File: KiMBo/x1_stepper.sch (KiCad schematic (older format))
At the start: 23 parts, among them U26 TMC2130

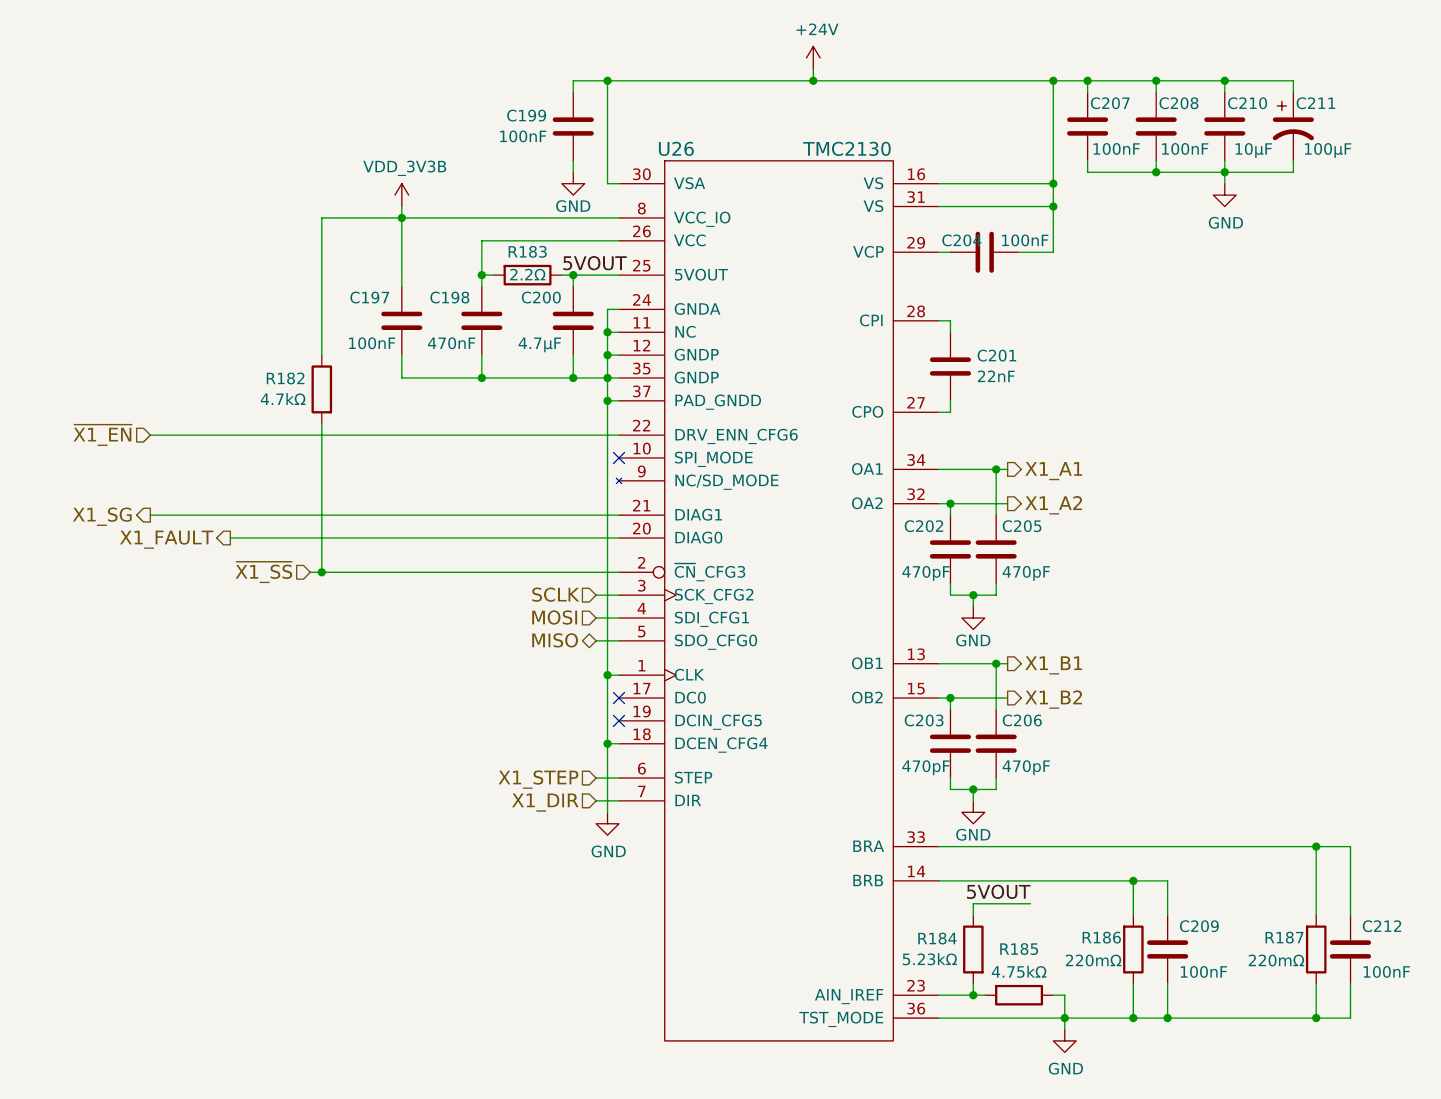
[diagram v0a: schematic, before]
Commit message: Leave SPI0 free for a display, reassign pins so SPI1 is available
Fix some typos/errors
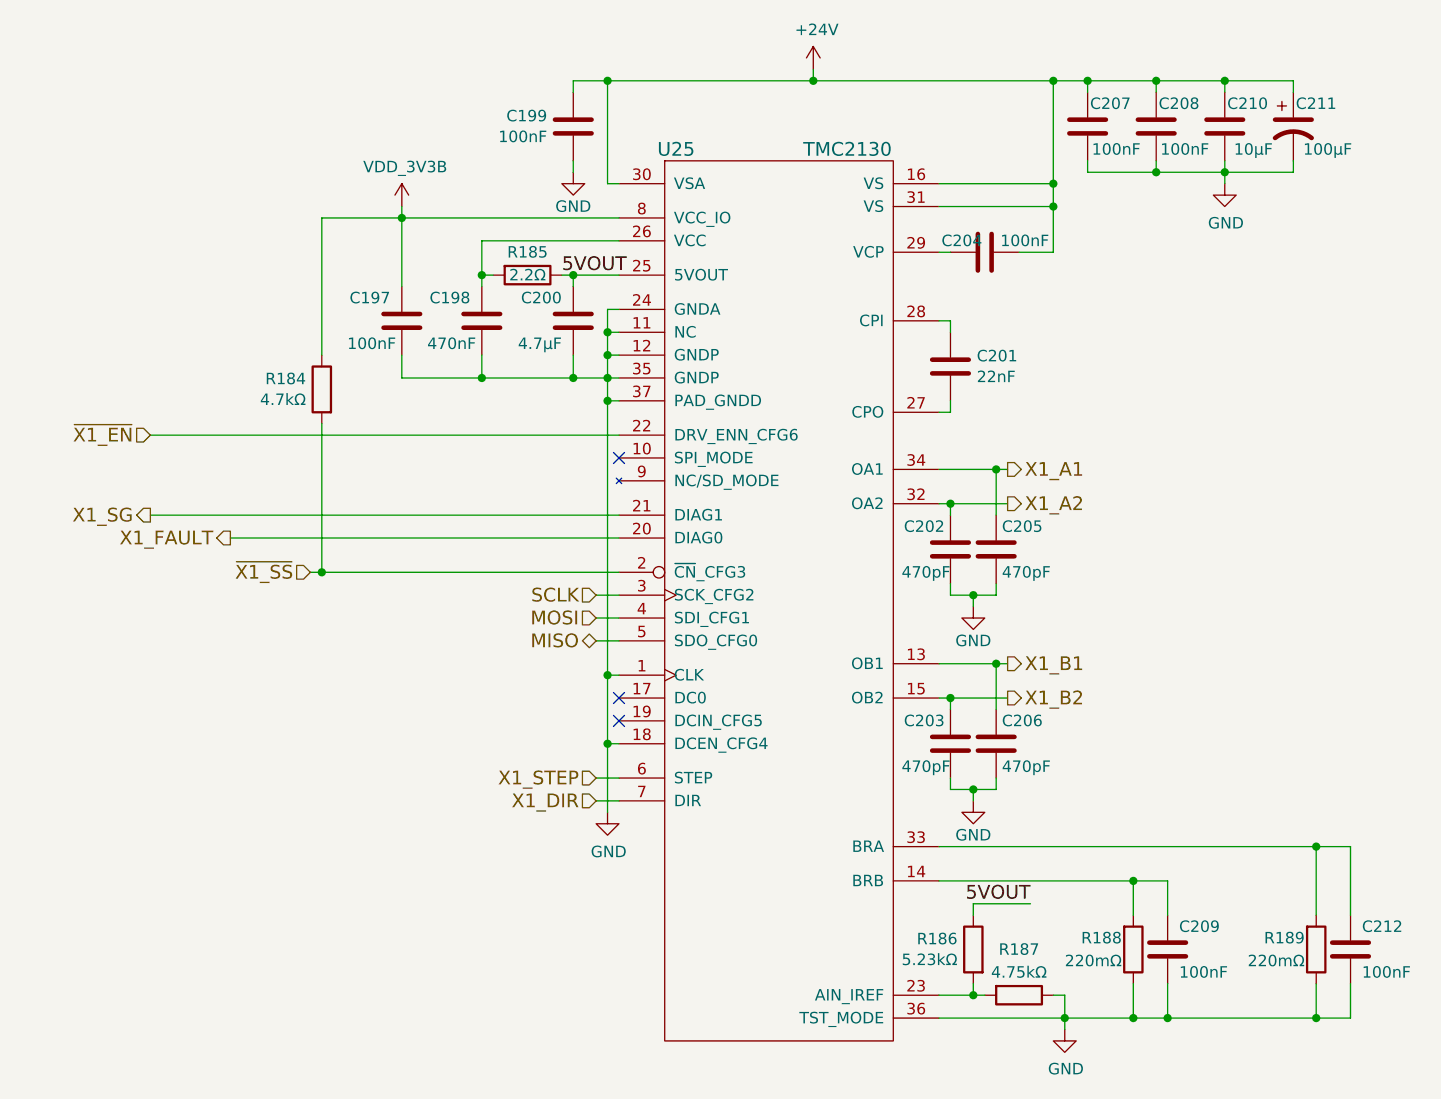
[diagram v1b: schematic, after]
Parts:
- renumbered R182 to R184, R183 to R185, R184 to R186, R185 to R187, R186 to R188, R187 to R189, U26 to U25
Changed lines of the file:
@@
 $EndComp
 $Comp
-L GND #PWR0256
+L GND #PWR0255
 U 1 1 5BA7E13F
 P 7500 3300
-F 0 "#PWR0256" H 7500 3050 50  0001 C CNN
+F 0 "#PWR0255" H 7500 3050 50  0001 C CNN
 F 1 "GND" H 7500 3150 50  0000 C CNN
 F 2 "" H 7500 3300 50  0000 C CNN
@@
 $EndComp
 $Comp
-L GND #PWR0257
+L GND #PWR0256
 U 1 1 58C092DF
 P 10350 3350
-F 0 "#PWR0257" H 10350 3100 50  0001 C CNN
+F 0 "#PWR0256" H 10350 3100 50  0001 C CNN
 F 1 "GND" H 10355 3177 50  0000 C CNN
 F 2 "" H 10350 3350 50  0000 C CNN
@@
 $EndComp
 $Comp
-L +24V #PWR0258
+L +24V #PWR0257
 U 1 1 5BA7E142
 P 8550 2850
-F 0 "#PWR0258" H 8550 2700 50  0001 C CNN
+F 0 "#PWR0257" H 8550 2700 50  0001 C CNN
 F 1 "+24V" H 8565 3023 50  0000 C CNN
 F 2 "" H 8550 2850 50  0000 C CNN
@@
 $EndComp
 $Comp
-L R R187
+L R R189
 U 1 1 5BA7E144
 P 10750 6700
-F 0 "R187" H 10700 6650 50  0000 R CNN
+F 0 "R189" H 10700 6650 50  0000 R CNN
 F 1 "220mΩ" H 10700 6750 50  0000 R CNN
 F 2 "" V 10680 6700 50  0001 C CNN
@@
 $EndComp
 $Comp
-L R R186
+L R R188
 U 1 1 5BA7E145
 P 9950 6700
-F 0 "R186" H 9900 6650 50  0000 R CNN
+F 0 "R188" H 9900 6650 50  0000 R CNN
 F 1 "220mΩ" H 9900 6750 50  0000 R CNN
 F 2 "" V 9880 6700 50  0001 C CNN
@@
 $EndComp
 $Comp
-L GND #PWR0259
+L GND #PWR0258
 U 1 1 58C09300
 P 9650 7050
-F 0 "#PWR0259" H 9650 6800 50  0001 C CNN
+F 0 "#PWR0258" H 9650 6800 50  0001 C CNN
 F 1 "GND" H 9655 6877 50  0000 C CNN
 F 2 "" H 9650 7050 50  0000 C CNN
@@
 NoConn ~ 7700 5600
 $Comp
-L R R183
+L R R185
 U 1 1 58C09307
 P 7300 3750
-F 0 "R183" V 7200 3750 50  0000 C CNN
+F 0 "R185" V 7200 3750 50  0000 C CNN
 F 1 "2.2Ω" V 7300 3750 50  0000 C CNN
 F 2 "" V 7230 3750 50  0001 C CNN
@@
 NoConn ~ 7700 5700
 $Comp
-L GND #PWR0260
+L GND #PWR0259
 U 1 1 58C09323
 P 7650 6100
-F 0 "#PWR0260" H 7650 5850 50  0001 C CNN
+F 0 "#PWR0259" H 7650 5850 50  0001 C CNN
 F 1 "GND" H 7655 5927 50  0000 C CNN
 F 2 "" H 7650 6100 50  0000 C CNN
@@
 5VOUT
 $Comp
-L R R184
+L R R186
 U 1 1 58C09343
 P 9250 6700
-F 0 "R184" H 9319 6746 50  0000 L CNN
+F 0 "R186" H 9319 6746 50  0000 L CNN
 F 1 "5.23kΩ" H 9319 6655 50  0000 L CNN
 F 2 "" V 9180 6700 50  0001 C CNN
@@
 5VOUT
 $Comp
-L R R185
+L R R187
 U 1 1 58C0934B
 P 9450 6900
-F 0 "R185" V 9250 6900 50  0000 C CNN
+F 0 "R187" V 9250 6900 50  0000 C CNN
 F 1 "4.75kΩ" V 9350 6900 50  0000 C CNN
 F 2 "" V 9380 6900 50  0001 C CNN
@@
 $EndComp
 $Comp
-L R R182
+L R R184
 U 1 1 5BA7E14F
 P 6400 4250
-F 0 "R182" H 6469 4296 50  0000 L CNN
+F 0 "R184" H 6469 4296 50  0000 L CNN
 F 1 "4.7kΩ" H 6469 4205 50  0000 L CNN
 F 2 "" V 6330 4250 50  0001 C CNN
@@
 $EndComp
 $Comp
-L GND #PWR0261
+L GND #PWR0260
 U 1 1 5BA7E152
 P 9250 5200
-F 0 "#PWR0261" H 9250 4950 50  0001 C CNN
+F 0 "#PWR0260" H 9250 4950 50  0001 C CNN
 F 1 "GND" H 9250 5050 50  0000 C CNN
 F 2 "" H 9250 5200 50  0000 C CNN
@@
 $EndComp
 $Comp
-L GND #PWR0262
+L GND #PWR0261
 U 1 1 5BA7E155
 P 9250 6050
-F 0 "#PWR0262" H 9250 5800 50  0001 C CNN
+F 0 "#PWR0261" H 9250 5800 50  0001 C CNN
 F 1 "GND" H 9250 5900 50  0000 C CNN
 F 2 "" H 9250 6050 50  0000 C CNN
@@
 $EndComp
 $Comp
-L TMC2130 U26
+L TMC2130 U25
 U 1 1 5BA7E157
 P 8400 4700
-F 0 "U26" H 7950 6200 60  0000 C CNN
+F 0 "U25" H 7950 6200 60  0000 C CNN
 F 1 "TMC2130" H 8700 6200 60  0000 C CNN
 F 2 "" H 8400 5000 60  0001 C CNN
@@
 	6400 3500 7700 3500
 $Comp
-L VDD_3V3B #PWR0263
+L VDD_3V3B #PWR0262
 U 1 1 5BA7E15A
 P 6750 3450
-F 0 "#PWR0263" H 6750 3300 50  0001 C CNN
+F 0 "#PWR0262" H 6750 3300 50  0001 C CNN
 F 1 "VDD_3V3B" H 6765 3623 50  0000 C CNN
 F 2 "" H 6750 3450 50  0000 C CNN

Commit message: Use fixed 5V LM2592HV Buck, include SPI0 header for LCD
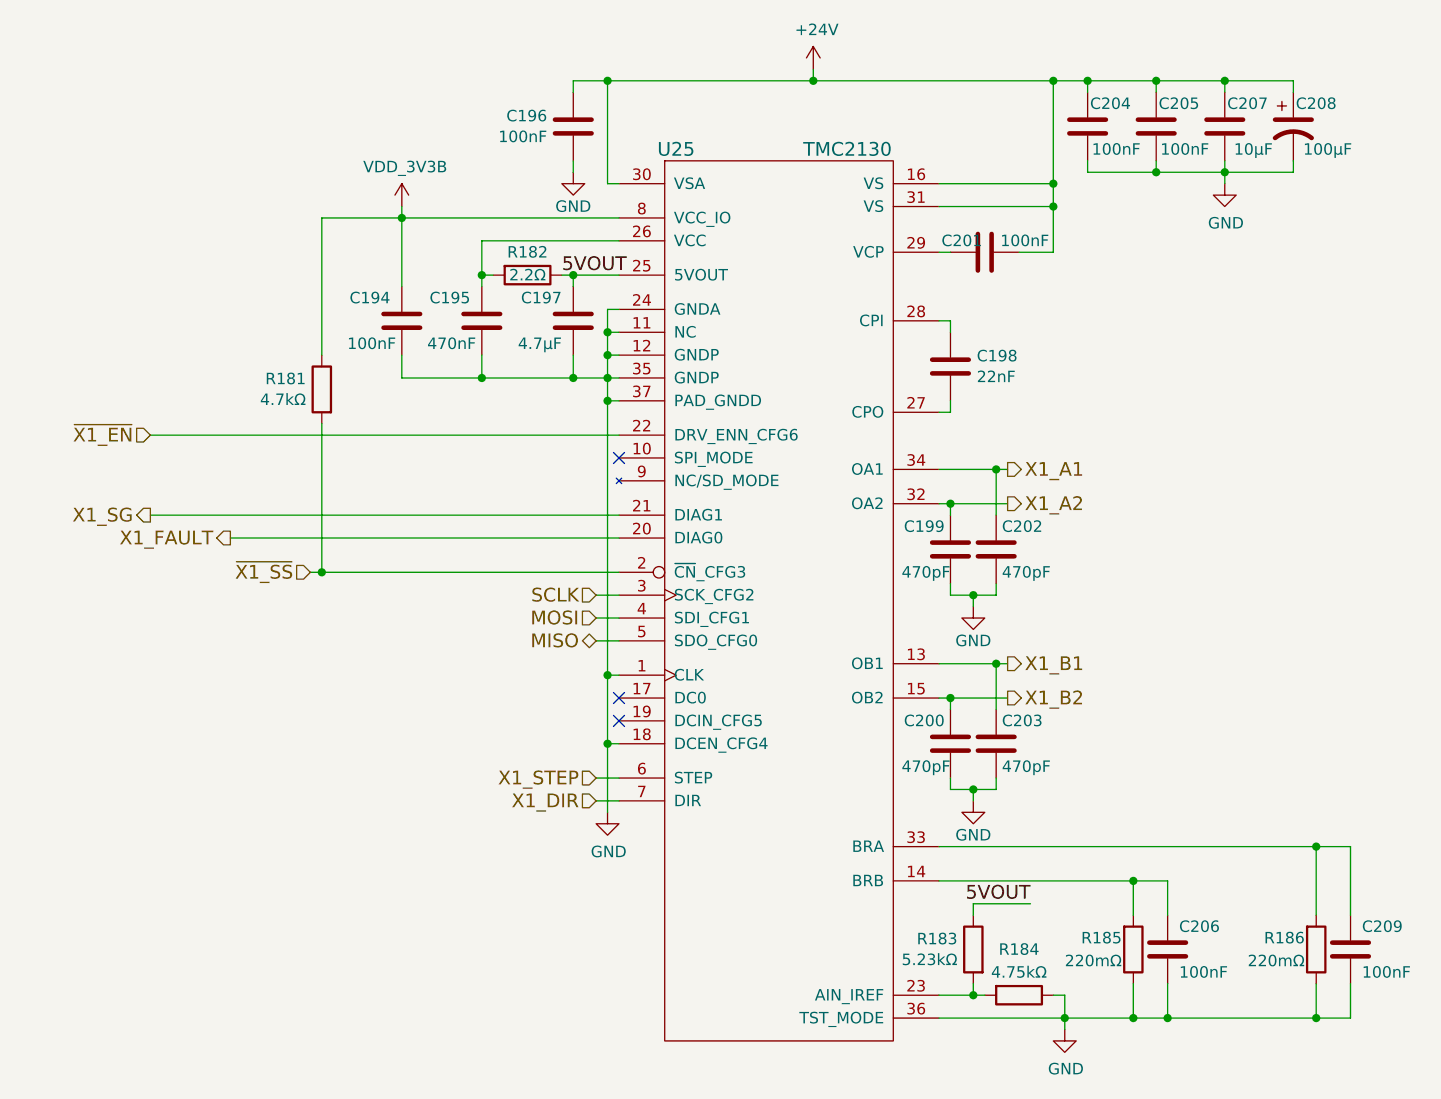
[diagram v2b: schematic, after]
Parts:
- renumbered C197 to C194, C198 to C195, C199 to C196, C200 to C197, C201 to C198, C202 to C199, C203 to C200, C204 to C201, C205 to C202, C206 to C203, C207 to C204, C208 to C205, C209 to C206, C210 to C207, C211 to C208, C212 to C209, R184 to R181, R185 to R182, R186 to R183, R187 to R184, R188 to R185, R189 to R186
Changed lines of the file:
@@
 X1_SG
 $Comp
-L C C199
+L C C196
 U 1 1 58C092B6
 P 7500 3100
-F 0 "C199" H 7386 3054 50  0000 R CNN
+F 0 "C196" H 7386 3054 50  0000 R CNN
 F 1 "100nF" H 7386 3145 50  0000 R CNN
 F 2 "Capacitors_SMD:C_0603" H 7538 2950 50  0001 C CNN
@@
 $EndComp
 $Comp
-L C C204
+L C C201
 U 1 1 58C092BD
 P 9300 3650
-F 0 "C204" V 9250 3550 50  0000 C CNN
+F 0 "C201" V 9250 3550 50  0000 C CNN
 F 1 "100nF" V 9250 3825 50  0000 C CNN
 F 2 "Capacitors_SMD:C_0603" H 9338 3500 50  0001 C CNN
@@
 $EndComp
 $Comp
-L CP1 C211
+L CP1 C208
 U 1 1 5BA7E13D
 P 10650 3100
-F 0 "C211" H 10750 3200 50  0000 C CNN
+F 0 "C208" H 10750 3200 50  0000 C CNN
 F 1 "100μF" H 10800 3000 50  0000 C CNN
 F 2 "Capacitors_SMD:c_elec_8x10" H 10650 3100 50  0001 C CNN
@@
 $EndComp
 $Comp
-L C C207
+L C C204
 U 1 1 5BA7E13E
 P 9750 3100
-F 0 "C207" H 9650 3200 50  0000 C CNN
+F 0 "C204" H 9650 3200 50  0000 C CNN
 F 1 "100nF" H 9625 3000 50  0000 C CNN
 F 2 "Capacitors_SMD:C_0603" H 9788 2950 50  0001 C CNN
@@
 $EndComp
 $Comp
-L GND #PWR0255
+L GND #PWR0250
 U 1 1 5BA7E13F
 P 7500 3300
-F 0 "#PWR0255" H 7500 3050 50  0001 C CNN
+F 0 "#PWR0250" H 7500 3050 50  0001 C CNN
 F 1 "GND" H 7500 3150 50  0000 C CNN
 F 2 "" H 7500 3300 50  0000 C CNN
@@
 $EndComp
 $Comp
-L C C208
+L C C205
 U 1 1 58C092D8
 P 10050 3100
-F 0 "C208" H 9950 3200 50  0000 C CNN
+F 0 "C205" H 9950 3200 50  0000 C CNN
 F 1 "100nF" H 9925 3000 50  0000 C CNN
 F 2 "Capacitors_SMD:C_0603" H 10088 2950 50  0001 C CNN
@@
 $EndComp
 $Comp
-L GND #PWR0256
+L GND #PWR0251
 U 1 1 58C092DF
 P 10350 3350
-F 0 "#PWR0256" H 10350 3100 50  0001 C CNN
+F 0 "#PWR0251" H 10350 3100 50  0001 C CNN
 F 1 "GND" H 10355 3177 50  0000 C CNN
 F 2 "" H 10350 3350 50  0000 C CNN
@@
 $EndComp
 $Comp
-L +24V #PWR0257
+L +24V #PWR0252
 U 1 1 5BA7E142
 P 8550 2850
-F 0 "#PWR0257" H 8550 2700 50  0001 C CNN
+F 0 "#PWR0252" H 8550 2700 50  0001 C CNN
 F 1 "+24V" H 8565 3023 50  0000 C CNN
 F 2 "" H 8550 2850 50  0000 C CNN
@@
 $EndComp
 $Comp
-L C C201
+L C C198
 U 1 1 5BA7E143
 P 9150 4150
-F 0 "C201" H 9265 4196 50  0000 L CNN
+F 0 "C198" H 9265 4196 50  0000 L CNN
 F 1 "22nF" H 9265 4105 50  0000 L CNN
 F 2 "Capacitors_SMD:C_0402" H 9188 4000 50  0001 C CNN
@@
 $EndComp
 $Comp
-L R R189
+L R R186
 U 1 1 5BA7E144
 P 10750 6700
-F 0 "R189" H 10700 6650 50  0000 R CNN
+F 0 "R186" H 10700 6650 50  0000 R CNN
 F 1 "220mΩ" H 10700 6750 50  0000 R CNN
 F 2 "" V 10680 6700 50  0001 C CNN
@@
 $EndComp
 $Comp
-L R R188
+L R R185
 U 1 1 5BA7E145
 P 9950 6700
-F 0 "R188" H 9900 6650 50  0000 R CNN
+F 0 "R185" H 9900 6650 50  0000 R CNN
 F 1 "220mΩ" H 9900 6750 50  0000 R CNN
 F 2 "" V 9880 6700 50  0001 C CNN
@@
 $EndComp
 $Comp
-L GND #PWR0258
+L GND #PWR0253
 U 1 1 58C09300
 P 9650 7050
-F 0 "#PWR0258" H 9650 6800 50  0001 C CNN
+F 0 "#PWR0253" H 9650 6800 50  0001 C CNN
 F 1 "GND" H 9655 6877 50  0000 C CNN
 F 2 "" H 9650 7050 50  0000 C CNN
@@
 NoConn ~ 7700 5600
 $Comp
-L R R185
+L R R182
 U 1 1 58C09307
 P 7300 3750
-F 0 "R185" V 7200 3750 50  0000 C CNN
+F 0 "R182" V 7200 3750 50  0000 C CNN
 F 1 "2.2Ω" V 7300 3750 50  0000 C CNN
 F 2 "" V 7230 3750 50  0001 C CNN
@@
 $EndComp
 $Comp
-L C C198
+L C C195
 U 1 1 58C0930E
 P 7100 3950
-F 0 "C198" H 7150 4050 50  0000 L CNN
+F 0 "C195" H 7150 4050 50  0000 L CNN
 F 1 "470nF" H 7125 3850 50  0000 L CNN
 F 2 "Capacitors_SMD:C_0603" H 7138 3800 50  0001 C CNN
@@
 NoConn ~ 7700 5700
 $Comp
-L GND #PWR0259
+L GND #PWR0254
 U 1 1 58C09323
 P 7650 6100
-F 0 "#PWR0259" H 7650 5850 50  0001 C CNN
+F 0 "#PWR0254" H 7650 5850 50  0001 C CNN
 F 1 "GND" H 7655 5927 50  0000 C CNN
 F 2 "" H 7650 6100 50  0000 C CNN
@@
 $EndComp
 $Comp
-L C C209
+L C C206
 U 1 1 58C09329
 P 10100 6700
-F 0 "C209" H 10150 6800 50  0000 L CNN
+F 0 "C206" H 10150 6800 50  0000 L CNN
 F 1 "100nF" H 10150 6600 50  0000 L CNN
 F 2 "Capacitors_SMD:C_0603" H 10138 6550 50  0001 C CNN
@@
 NoConn ~ 7700 4550
 $Comp
-L C C200
+L C C197
 U 1 1 58C0933B
 P 7500 3950
-F 0 "C200" H 7550 4050 50  0000 L CNN
+F 0 "C197" H 7550 4050 50  0000 L CNN
 F 1 "4.7μF" H 7550 3850 50  0000 L CNN
 F 2 "Capacitors_SMD:C_0402" H 7538 3800 50  0001 C CNN
@@
 5VOUT
 $Comp
-L R R186
+L R R183
 U 1 1 58C09343
 P 9250 6700
-F 0 "R186" H 9319 6746 50  0000 L CNN
+F 0 "R183" H 9319 6746 50  0000 L CNN
 F 1 "5.23kΩ" H 9319 6655 50  0000 L CNN
 F 2 "" V 9180 6700 50  0001 C CNN
@@
 5VOUT
 $Comp
-L R R187
+L R R184
 U 1 1 58C0934B
 P 9450 6900
-F 0 "R187" V 9250 6900 50  0000 C CNN
+F 0 "R184" V 9250 6900 50  0000 C CNN
 F 1 "4.75kΩ" V 9350 6900 50  0000 C CNN
 F 2 "" V 9380 6900 50  0001 C CNN
@@
 $EndComp
 $Comp
-L R R184
+L R R181
 U 1 1 5BA7E14F
 P 6400 4250
-F 0 "R184" H 6469 4296 50  0000 L CNN
+F 0 "R181" H 6469 4296 50  0000 L CNN
 F 1 "4.7kΩ" H 6469 4205 50  0000 L CNN
 F 2 "" V 6330 4250 50  0001 C CNN
@@
 $EndComp
 $Comp
-L C C212
+L C C209
 U 1 1 5BA7E150
 P 10900 6700
-F 0 "C212" H 10950 6800 50  0000 L CNN
+F 0 "C209" H 10950 6800 50  0000 L CNN
 F 1 "100nF" H 10950 6600 50  0000 L CNN
 F 2 "Capacitors_SMD:C_0603" H 10938 6550 50  0001 C CNN
@@
 $EndComp
 $Comp
-L C C202
+L C C199
 U 1 1 5BA7E151
 P 9150 4950
-F 0 "C202" H 9175 5050 50  0000 L CNN
+F 0 "C199" H 9175 5050 50  0000 L CNN
 F 1 "470pF" H 9150 4850 50  0000 L CNN
 F 2 "Capacitors_SMD:C_0603" H 9188 4800 50  0001 C CNN
@@
 $EndComp
 $Comp
-L GND #PWR0260
+L GND #PWR0255
 U 1 1 5BA7E152
 P 9250 5200
-F 0 "#PWR0260" H 9250 4950 50  0001 C CNN
+F 0 "#PWR0255" H 9250 4950 50  0001 C CNN
 F 1 "GND" H 9250 5050 50  0000 C CNN
 F 2 "" H 9250 5200 50  0000 C CNN
@@
 $EndComp
 $Comp
-L C C205
+L C C202
 U 1 1 5BA7E153
 P 9350 4950
-F 0 "C205" H 9375 5050 50  0000 L CNN
+F 0 "C202" H 9375 5050 50  0000 L CNN
 F 1 "470pF" H 9375 4850 50  0000 L CNN
 F 2 "Capacitors_SMD:C_0603" H 9388 4800 50  0001 C CNN
@@
 $EndComp
 $Comp
-L C C203
+L C C200
 U 1 1 58C09377
 P 9150 5800
-F 0 "C203" H 9175 5900 50  0000 L CNN
+F 0 "C200" H 9175 5900 50  0000 L CNN
 F 1 "470pF" H 9150 5700 50  0000 L CNN
 F 2 "Capacitors_SMD:C_0603" H 9188 5650 50  0001 C CNN
@@
 $EndComp
 $Comp
-L GND #PWR0261
+L GND #PWR0256
 U 1 1 5BA7E155
 P 9250 6050
-F 0 "#PWR0261" H 9250 5800 50  0001 C CNN
+F 0 "#PWR0256" H 9250 5800 50  0001 C CNN
 F 1 "GND" H 9250 5900 50  0000 C CNN
 F 2 "" H 9250 6050 50  0000 C CNN
@@
 $EndComp
 $Comp
-L C C206
+L C C203
 U 1 1 5BA7E156
 P 9350 5800
-F 0 "C206" H 9375 5900 50  0000 L CNN
+F 0 "C203" H 9375 5900 50  0000 L CNN
 F 1 "470pF" H 9375 5700 50  0000 L CNN
 F 2 "Capacitors_SMD:C_0603" H 9388 5650 50  0001 C CNN
@@
 	9150 6000 9150 5950
 $Comp
-L C C210
+L C C207
 U 1 1 58C0940A
 P 10350 3100
-F 0 "C210" H 10250 3200 50  0000 C CNN
+F 0 "C207" H 10250 3200 50  0000 C CNN
 F 1 "10μF" H 10225 3000 50  0000 C CNN
 F 2 "Capacitors_SMD:C_0805" H 10388 2950 50  0001 C CNN
@@
 	6400 3500 7700 3500
 $Comp
-L VDD_3V3B #PWR0262
+L VDD_3V3B #PWR0257
 U 1 1 5BA7E15A
 P 6750 3450
-F 0 "#PWR0262" H 6750 3300 50  0001 C CNN
+F 0 "#PWR0257" H 6750 3300 50  0001 C CNN
 F 1 "VDD_3V3B" H 6765 3623 50  0000 C CNN
 F 2 "" H 6750 3450 50  0000 C CNN
@@
 $EndComp
 $Comp
-L C C197
+L C C194
 U 1 1 5A89A0A1
 P 6750 3950
-F 0 "C197" H 6800 4050 50  0000 L CNN
+F 0 "C194" H 6800 4050 50  0000 L CNN
 F 1 "100nF" H 6775 3850 50  0000 L CNN
 F 2 "Capacitors_SMD:C_0603" H 6788 3800 50  0001 C CNN

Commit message: Assocate more footprints
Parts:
- C197, C198: footprint Capacitors_SMD:C_0402 -> Capacitors_SMD:C_0603
- R181, R182, R183, R184: footprint (none) -> Resistors_SMD:R_0603
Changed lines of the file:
@@
 F 0 "C198" H 9265 4196 50  0000 L CNN
 F 1 "22nF" H 9265 4105 50  0000 L CNN
-F 2 "Capacitors_SMD:C_0402" H 9188 4000 50  0001 C CNN
+F 2 "Capacitors_SMD:C_0603" H 9188 4000 50  0001 C CNN
 F 3 "" H 9150 4150 50  0000 C CNN
 	1    9150 4150
@@
 F 0 "R182" V 7200 3750 50  0000 C CNN
 F 1 "2.2Ω" V 7300 3750 50  0000 C CNN
-F 2 "" V 7230 3750 50  0001 C CNN
+F 2 "Resistors_SMD:R_0603" V 7230 3750 50  0001 C CNN
 F 3 "" H 7300 3750 50  0000 C CNN
 	1    7300 3750
@@
 F 0 "C197" H 7550 4050 50  0000 L CNN
 F 1 "4.7μF" H 7550 3850 50  0000 L CNN
-F 2 "Capacitors_SMD:C_0402" H 7538 3800 50  0001 C CNN
+F 2 "Capacitors_SMD:C_0603" H 7538 3800 50  0001 C CNN
 F 3 "" H 7500 3950 50  0000 C CNN
 	1    7500 3950
@@
 F 0 "R183" H 9319 6746 50  0000 L CNN
 F 1 "5.23kΩ" H 9319 6655 50  0000 L CNN
-F 2 "" V 9180 6700 50  0001 C CNN
+F 2 "Resistors_SMD:R_0603" V 9180 6700 50  0001 C CNN
 F 3 "" H 9250 6700 50  0000 C CNN
 	1    9250 6700
@@
 F 0 "R184" V 9250 6900 50  0000 C CNN
 F 1 "4.75kΩ" V 9350 6900 50  0000 C CNN
-F 2 "" V 9380 6900 50  0001 C CNN
+F 2 "Resistors_SMD:R_0603" V 9380 6900 50  0001 C CNN
 F 3 "" H 9450 6900 50  0000 C CNN
 	1    9450 6900
@@
 F 0 "R181" H 6469 4296 50  0000 L CNN
 F 1 "4.7kΩ" H 6469 4205 50  0000 L CNN
-F 2 "" V 6330 4250 50  0001 C CNN
+F 2 "Resistors_SMD:R_0603" V 6330 4250 50  0001 C CNN
 F 3 "" H 6400 4250 50  0000 C CNN
 	1    6400 4250
